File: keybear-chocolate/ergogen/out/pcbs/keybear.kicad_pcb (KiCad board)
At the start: 2 copper layers, 148.5 x 139.2 mm, 24 parts

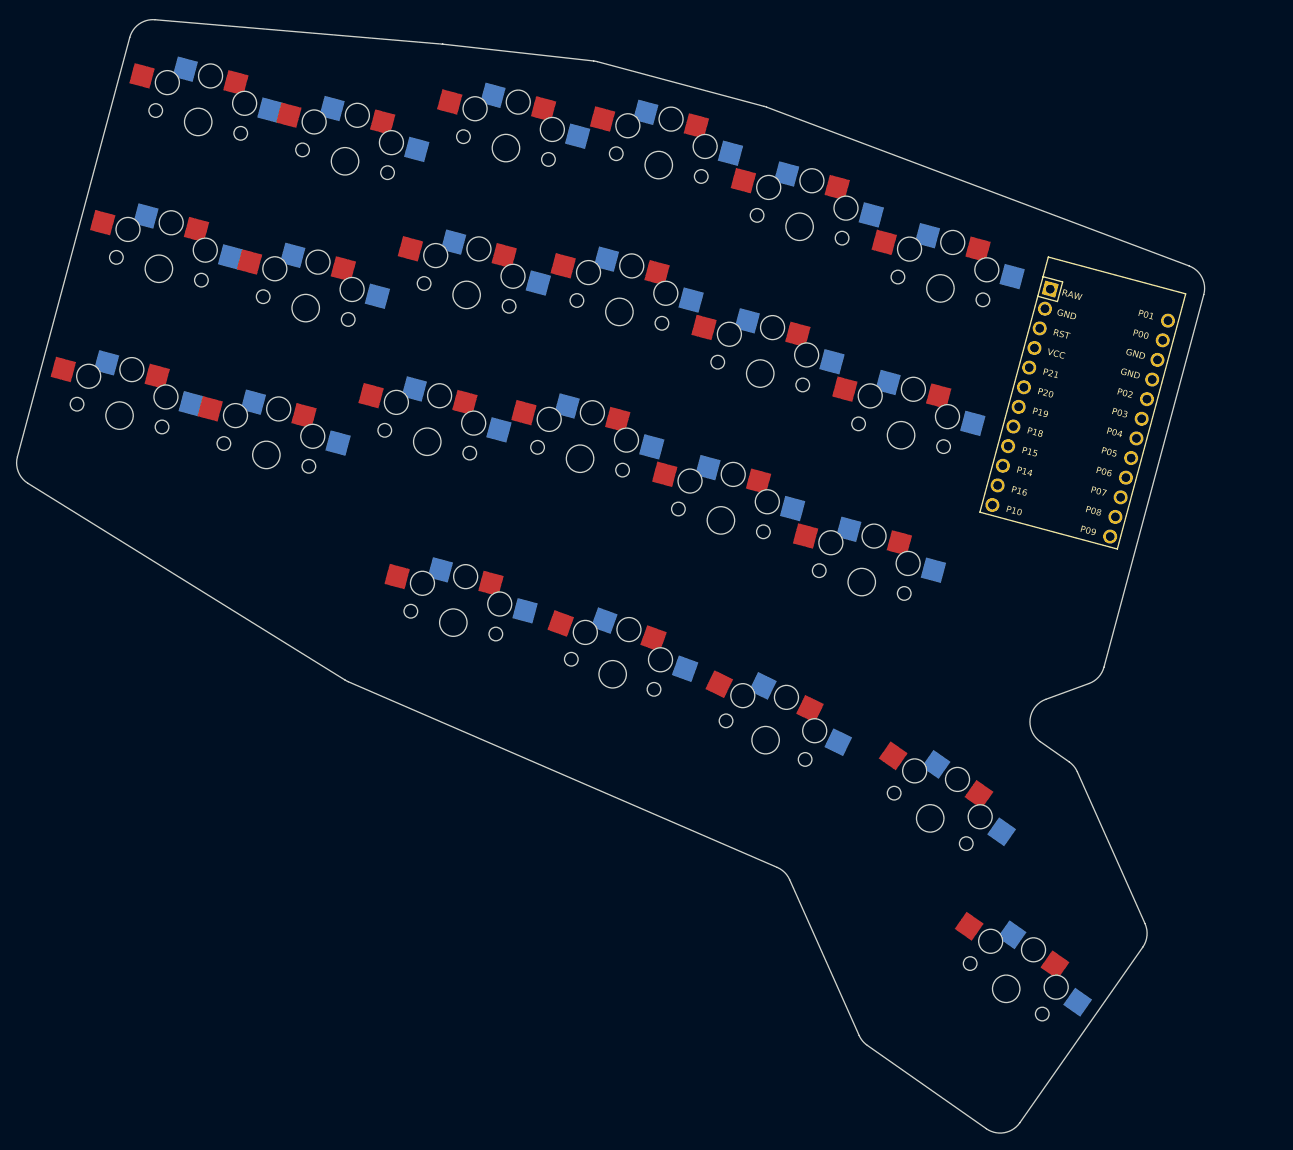
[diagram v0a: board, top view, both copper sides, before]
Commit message: adjust switch pos
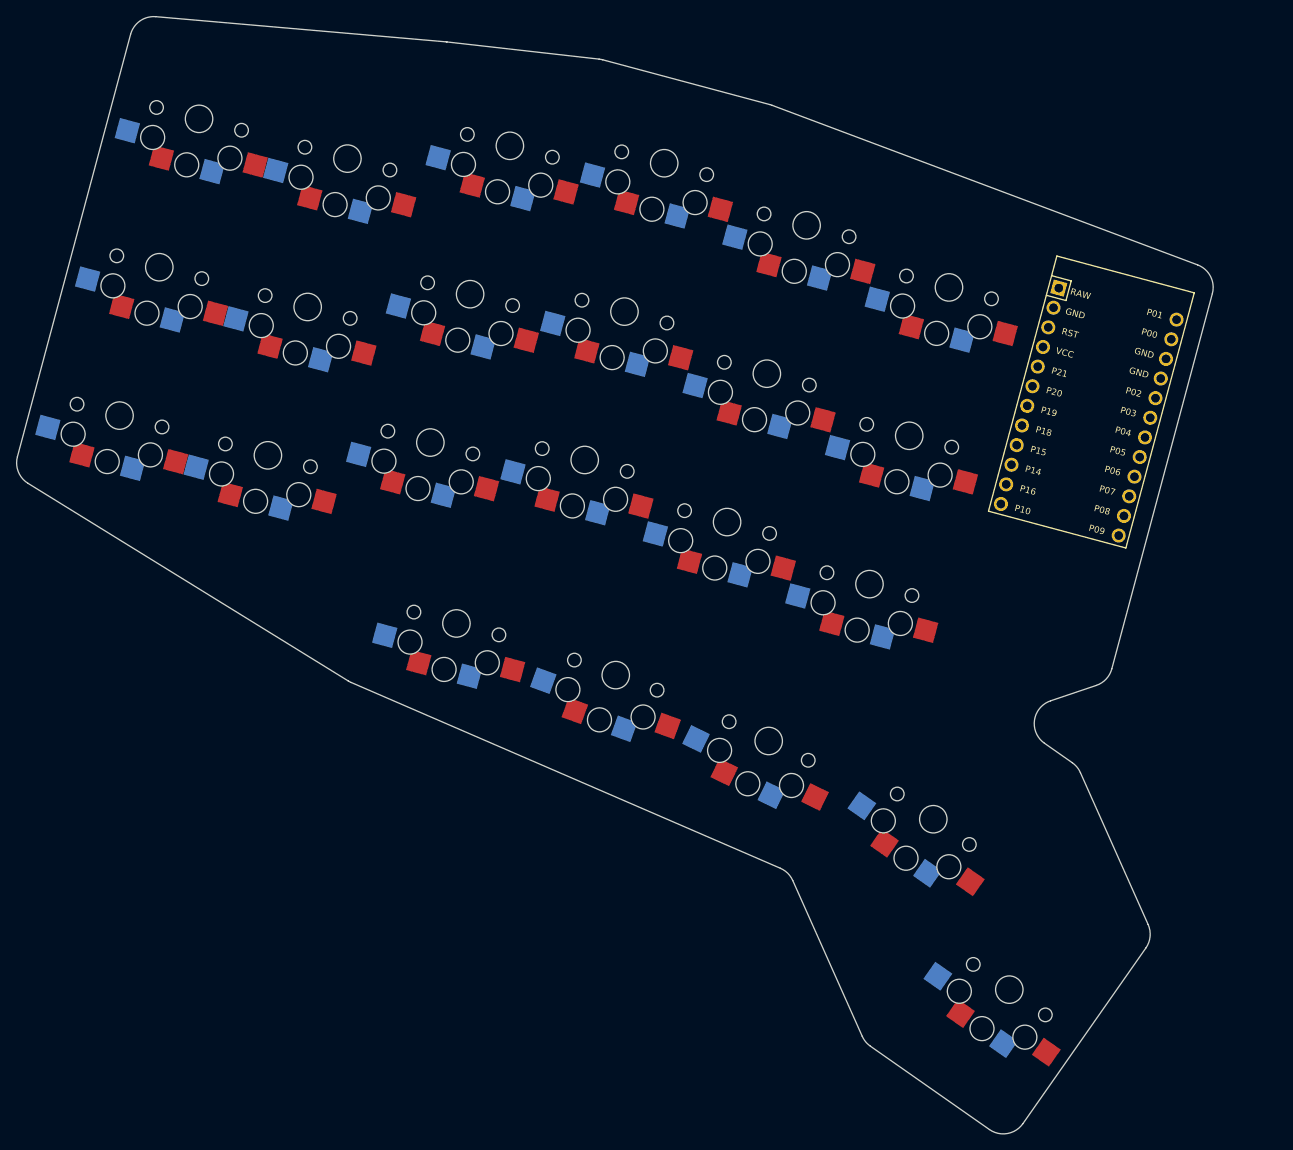
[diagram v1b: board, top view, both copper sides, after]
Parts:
- moved S18 1.08 mm to (249.4, 116.2), turned to 165 degrees
- moved MCU1 1.08 mm to (266.9, 131.8)
- moved S17 1.02 mm to (244.5, 134.8), turned to 165 degrees
- moved S16 1.00 mm to (239.5, 153.3), turned to 165 degrees
- moved S15 0.89 mm to (231.6, 108.4), turned to 165 degrees
- moved S14 0.82 mm to (226.7, 127.0), turned to 165 degrees
- moved S13 0.80 mm to (221.7, 145.5), turned to 165 degrees
- moved S12 0.72 mm to (213.8, 100.7), turned to 165 degrees
- moved S11 0.63 mm to (208.9, 119.2), turned to 165 degrees
- moved S10 0.60 mm to (203.9, 137.8), turned to 165 degrees
- moved S9 0.57 mm to (194.5, 98.5), turned to 165 degrees
- moved S8 0.45 mm to (189.6, 117.1), turned to 165 degrees
- moved S6 0.45 mm to (174.2, 100.1), turned to 165 degrees
- moved S22 0.40 mm to (247.5, 182.7), turned to 145 degrees
- moved S23 0.40 mm to (257.0, 204.0), turned to 145 degrees
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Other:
- board size 148.5 x 139.2 mm -> 149.6 x 139.7 mm

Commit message: latest ergogen output
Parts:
- added ?: , Button_Switch_SMD:SW_SPDT_PCM12, F.Cu at (251.0, 141.1)
- added D1: , ComboDiode, F.Cu at (158.1, 148.4)
- added D10: , ComboDiode, F.Cu at (215.7, 138.7)
- added D11: , ComboDiode, F.Cu at (215.7, 119.5)
- added D12: , ComboDiode, F.Cu at (215.7, 100.3)
- added D13: , ComboDiode, F.Cu at (234.9, 141.6)
- added D14: , ComboDiode, F.Cu at (234.9, 122.4)
- added D15: , ComboDiode, F.Cu at (234.9, 103.2)
- added D16: , ComboDiode, F.Cu at (254.1, 144.5)
- added D17: , ComboDiode, F.Cu at (254.1, 125.3)
- added D18: , ComboDiode, F.Cu at (254.1, 106.1)
- added D19: , ComboDiode, F.Cu at (205.5, 162.6)
- added D2: , ComboDiode, F.Cu at (158.1, 129.2)
- added D20: , ComboDiode, F.Cu at (226.5, 164.4)
- added D21: , ComboDiode, F.Cu at (247.2, 168.3)
- added D22: , ComboDiode, F.Cu at (262.6, 164.3)
- added D23: , ComboDiode, F.Cu at (277.3, 182.4)
- added D3: , ComboDiode, F.Cu at (158.1, 110.0)
- added D4: , ComboDiode, F.Cu at (177.3, 148.4)
- added D5: , ComboDiode, F.Cu at (177.3, 129.2)
- added D6: , ComboDiode, F.Cu at (177.3, 110.0)
- added D7: , ComboDiode, F.Cu at (196.5, 141.6)
- added D8: , ComboDiode, F.Cu at (196.5, 122.4)
- added D9: , ComboDiode, F.Cu at (196.5, 103.2)
- moved S23 23.3 mm to (276.0, 190.5), turned to 250 degrees
- moved S1 18.3 mm to (150.0, 150.0), turned to 180 degrees
- moved MCU1 17.8 mm to (266.9, 114.0), turned to -90 degrees
- moved S3 17.4 mm to (150.0, 111.6), turned to 180 degrees
- moved S22 17.2 mm to (261.3, 172.4), turned to 250 degrees
- moved S2 17.1 mm to (150.0, 130.8), turned to 180 degrees
- moved S4 13.7 mm to (169.2, 150.0), turned to 180 degrees
- moved S21 12.9 mm to (238.9, 168.3), turned to 169 degrees
- moved S6 12.5 mm to (169.2, 111.6), turned to 180 degrees
- moved S5 12.1 mm to (169.2, 130.8), turned to 180 degrees
- moved S19 11.3 mm to (197.4, 164.2), turned to 180 degrees
- moved S20 10.6 mm to (218.3, 165.3), turned to 175 degrees
- moved S16 9.72 mm to (246.0, 146.1), turned to 180 degrees
- moved S18 9.18 mm to (246.0, 107.7), turned to 180 degrees
- moved S9 8.79 mm to (188.4, 104.8), turned to 180 degrees
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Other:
- board size 149.6 x 139.7 mm -> 151.4 x 117.1 mm

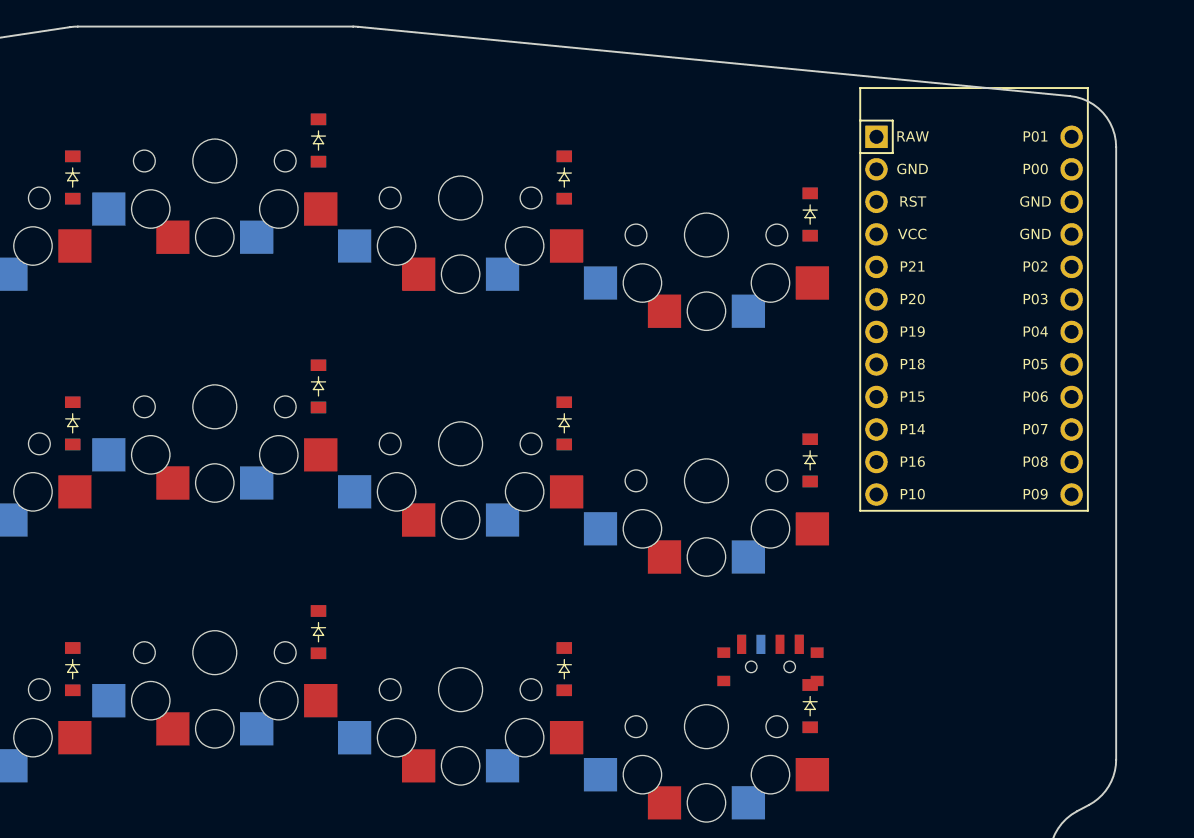
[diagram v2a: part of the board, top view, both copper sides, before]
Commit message: outline updated
updated the outline to fit the promicro
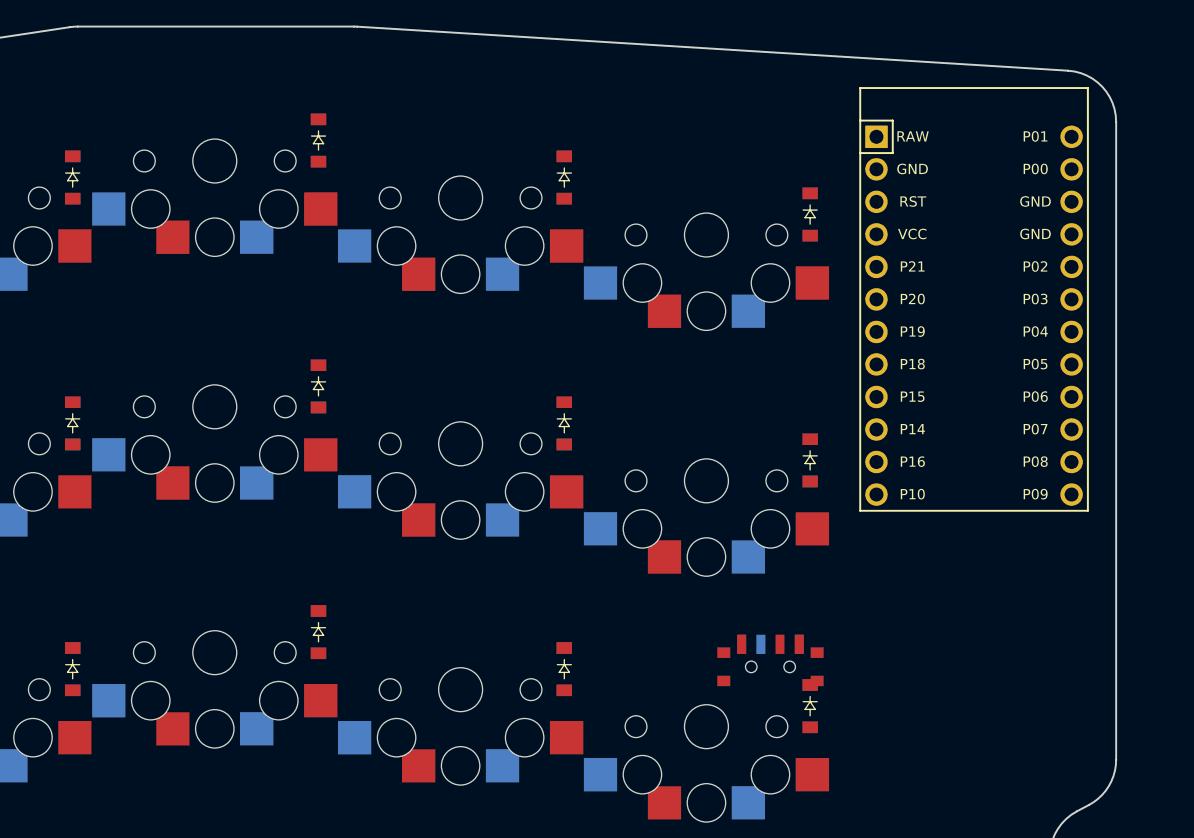
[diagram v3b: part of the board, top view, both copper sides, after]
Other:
- outline, holes or cut-outs redrawn
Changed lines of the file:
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@@
 (gr_line (start 142.30251837674913 100.51517903745068) (end 177.34905522969035 94.30902146974232) (angle 90) (layer Edge.Cuts) (width 0.15))
 (gr_line (start 177.45116046544442 94.29229928410757) (end 196.3039792958942 91.45455728306591) (angle 90) (layer Edge.Cuts) (width 0.15))
-(gr_line (start 196.89935568339106 91.41) (end 218.4058452487889 91.41) (angle 90) (layer Edge.Cuts) (width 0.15))
-(gr_line (start 218.7932412478509 91.42880360963936) (end 274.38739599906216 96.83847051977406) (angle 90) (layer Edge.Cuts) (width 0.15))
-(gr_line (start 278 148.67538883236938) (end 278 100.81966691013469) (angle 90) (layer Edge.Cuts) (width 0.15))
+(gr_line (start 196.89935568339106 91.41) (end 218.47621318586943 91.41) (angle 90) (layer Edge.Cuts) (width 0.15))
+(gr_line (start 218.72355039204098 91.41765430038234) (end 274.2473372061715 94.8575117999783) (angle 90) (layer Edge.Cuts) (width 0.15))
+(gr_line (start 278 148.67538883236938) (end 278 98.84985749959597) (angle 90) (layer Edge.Cuts) (width 0.15))
 (gr_line (start 275.8633973258458 152.2148450714089) (end 274.9500022888942 152.69571496733892) (angle 90) (layer Edge.Cuts) (width 0.15))
 (gr_line (start 275.445319159205 159.99394175895947) (end 276.8229855 160.49537129999996) (angle 90) (layer Edge.Cuts) (width 0.15))
@@
 (gr_arc (start 178.04653685294122 98.24774200104164) (end 177.45116045294122 94.29229930104164) (angle -1.482075501189442) (layer Edge.Cuts) (width 0.15))
 (gr_arc (start 196.89935568339106 95.41) (end 196.89935568339106 91.41) (angle -8.559946194970777) (layer Edge.Cuts) (width 0.15))
-(gr_arc (start 218.4058452487889 95.41) (end 218.7932412487889 91.4288037) (angle -5.557750441598785) (layer Edge.Cuts) (width 0.15))
-(gr_arc (start 274 100.81966691013469) (end 278 100.81966691013469) (angle -84.44224955839874) (layer Edge.Cuts) (width 0.15))
+(gr_arc (start 218.47621318586943 95.41) (end 218.72355038586943 91.4176543) (angle -3.54510608067136) (layer Edge.Cuts) (width 0.15))
+(gr_arc (start 274 98.84985749959597) (end 278 98.84985749959597) (angle -86.45489391932946) (layer Edge.Cuts) (width 0.15))
 (gr_arc (start 274 148.67538883236938) (end 275.8633973 152.21484503236937) (angle -62.234796878406655) (layer Edge.Cuts) (width 0.15))
 (gr_arc (start 276.81339961474 156.2351712063785) (end 274.95000231474 152.69571500637852) (angle -132.23479880375217) (layer Edge.Cuts) (width 0.15))

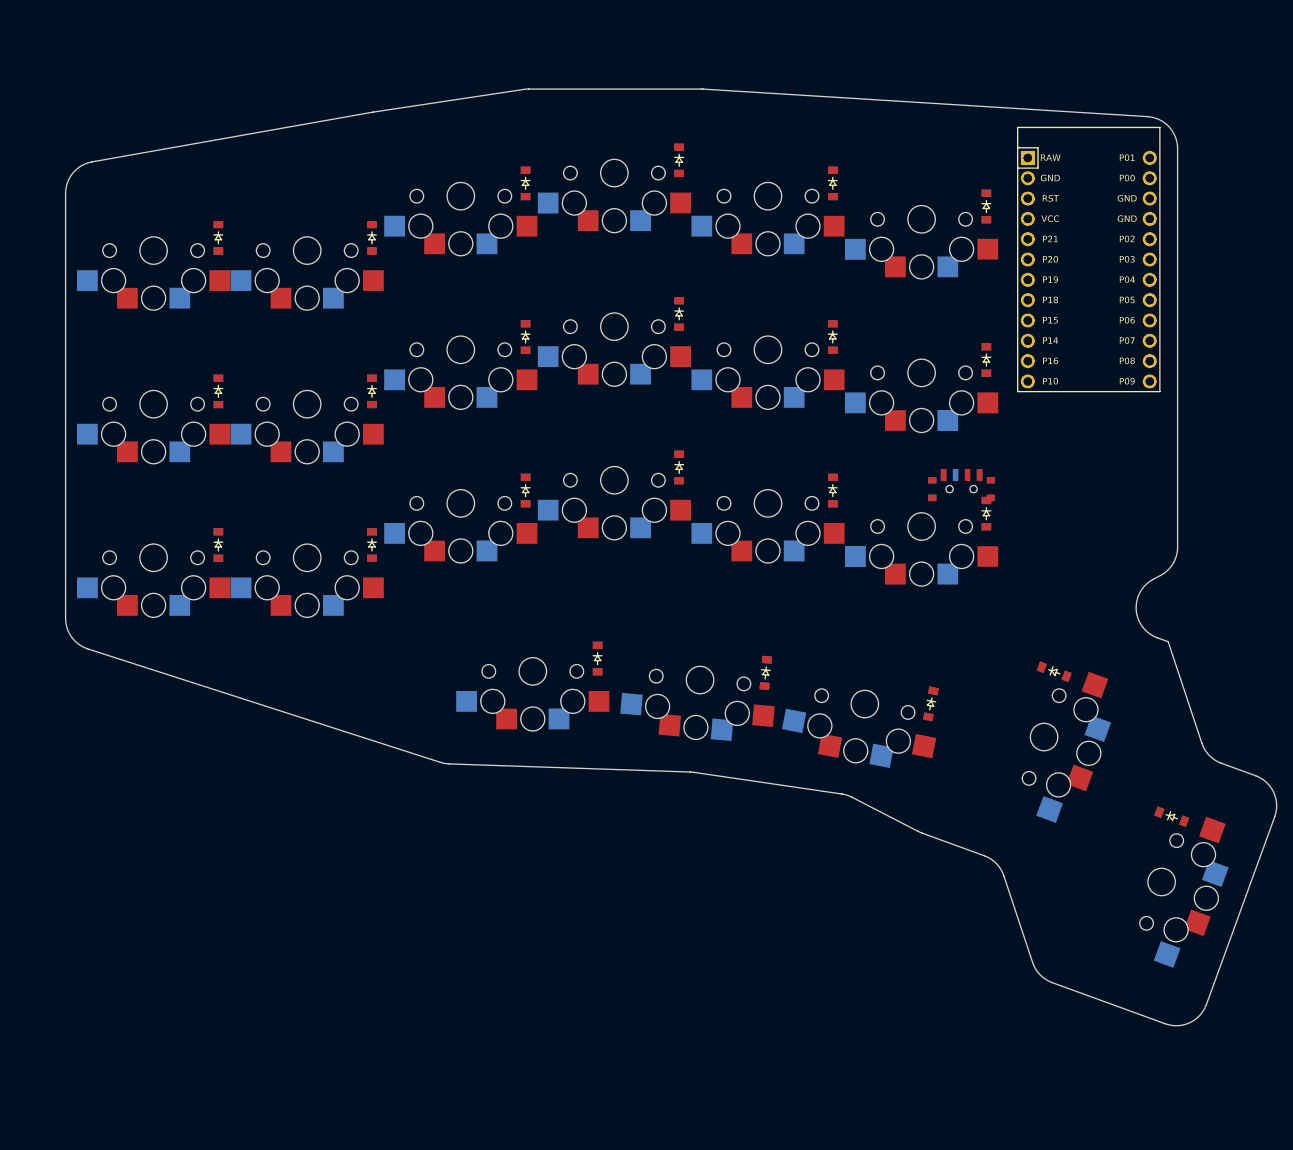
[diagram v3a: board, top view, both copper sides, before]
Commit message: deleting key and making the keyboard more compact - ergogen
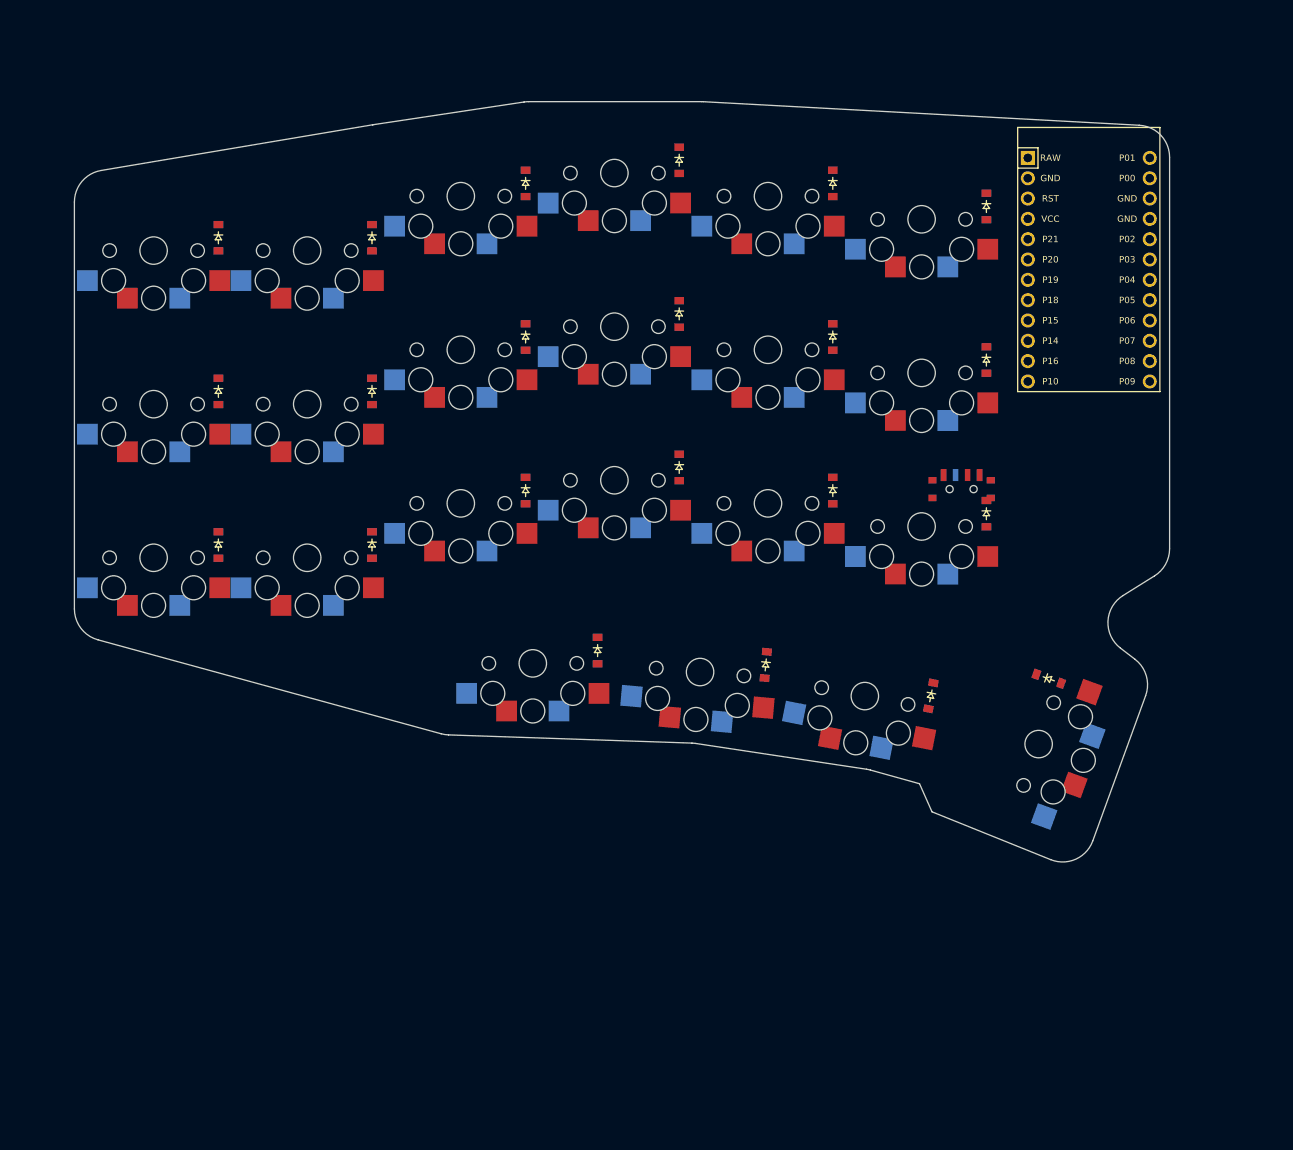
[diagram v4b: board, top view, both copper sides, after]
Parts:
- removed D23: , ComboDiode
- removed S23: , PG1350
- moved D22 1.11 mm to (261.9, 165.1)
- moved S22 1.11 mm to (260.6, 173.3)
- moved D19 1.00 mm to (205.5, 161.6)
- moved D20 1.00 mm to (226.5, 163.4)
- moved D21 1.00 mm to (247.2, 167.3)
- moved S19 1.00 mm to (197.4, 163.2)
- moved S20 1.00 mm to (218.3, 164.3)
- moved S21 1.00 mm to (238.9, 167.3)
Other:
- board size 151.4 x 117.1 mm -> 136.9 x 95 mm
